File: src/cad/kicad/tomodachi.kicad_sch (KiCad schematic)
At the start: 10 parts, among them SW1 SW_SPST, U1 XIAO-ESP32-C3-DIP, U2 KY-040, U3 TC00500

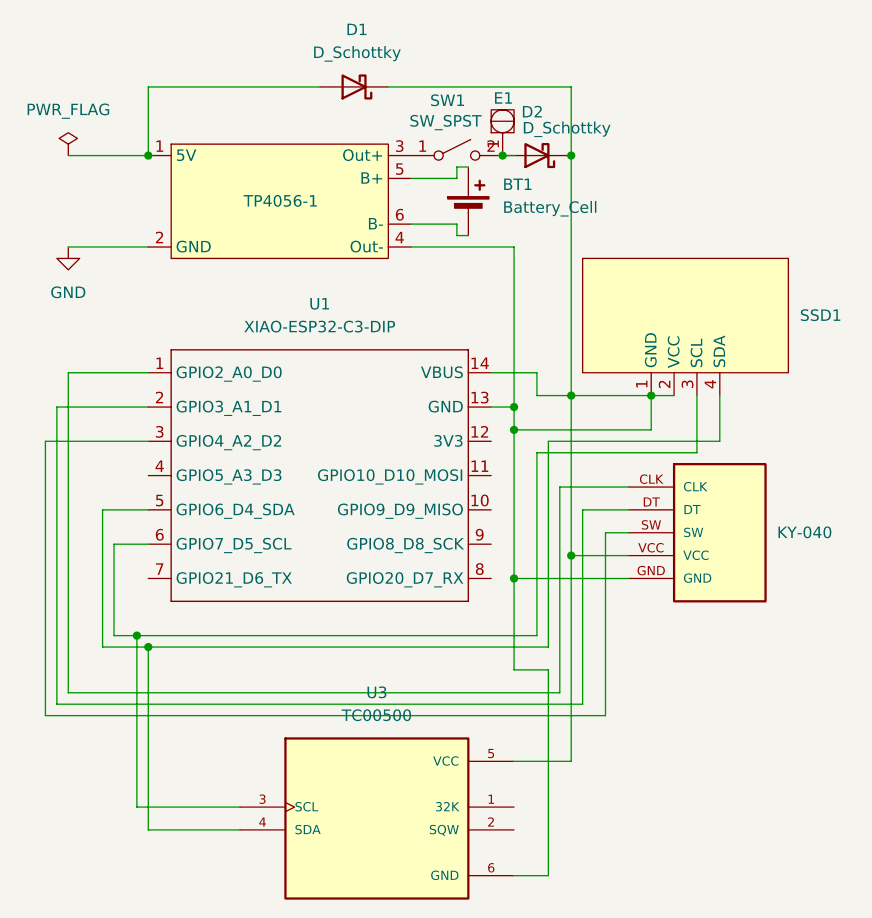
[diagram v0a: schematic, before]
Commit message: fixed PCB & added BOM and 3D files
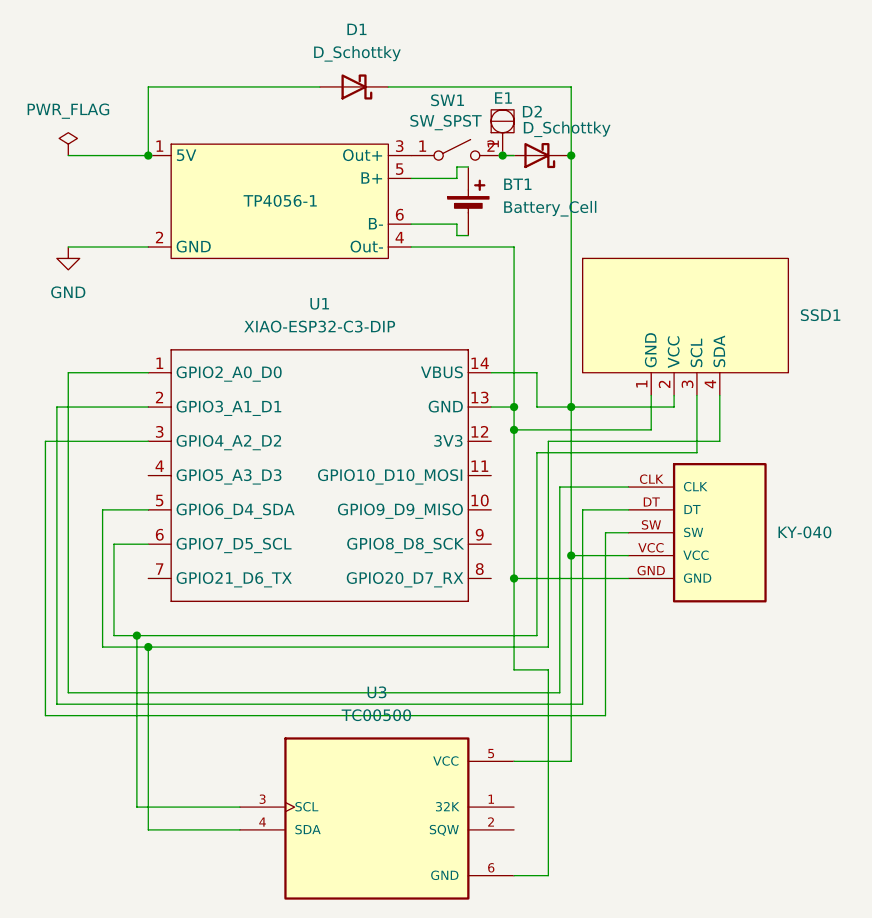
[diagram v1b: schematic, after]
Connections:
- net at D1.1 (K), D2.1 (K), SSD1.2 (VCC)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: no longer SSD1.1 (GND), TP4056-1.4 (Out-), U1.13 (GND), U2.GND, U3.6 (GND)
- new net: SSD1.1 (GND), TP4056-1.4 (Out-), U1.13 (GND), U2.GND, U3.6 (GND)
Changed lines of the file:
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@@
 	(paper "A4")
 	(junction
-		(at 120.65 81.28)
-		(diameter 0)
-		(color 0 0 0 0)
-	)
-	(junction
 		(at 113.03 54.61)
 		(diameter 0)
@@
 	)
 	(junction
+		(at 120.65 82.55)
+		(diameter 0)
+		(color 0 0 0 0)
+	)
+	(junction
 		(at 120.65 54.61)
 		(diameter 0)
@@
 	)
 	(junction
-		(at 129.54 81.28)
-		(diameter 0)
-		(color 0 0 0 0)
-	)
-	(junction
 		(at 73.66 54.61)
 		(diameter 0)
@@
 	(wire
 		(pts
+			(xy 132.08 81.28) (xy 132.08 82.55)
+		)
+		(stroke
+			(width 0)
+			(type default)
+		)
+	)
+	(wire
+		(pts
 			(xy 114.3 82.55) (xy 114.3 85.09)
 		)
@@
 	(wire
 		(pts
+			(xy 132.08 82.55) (xy 120.65 82.55)
+		)
+		(stroke
+			(width 0)
+			(type default)
+		)
+	)
+	(wire
+		(pts
 			(xy 114.3 54.61) (xy 113.03 54.61)
 		)
@@
 	(wire
 		(pts
+			(xy 120.65 82.55) (xy 120.65 99.06)
+		)
+		(stroke
+			(width 0)
+			(type default)
+		)
+	)
+	(wire
+		(pts
 			(xy 111.76 82.55) (xy 114.3 82.55)
 		)
@@
 	(wire
 		(pts
-			(xy 120.65 81.28) (xy 129.54 81.28)
-		)
-		(stroke
-			(width 0)
-			(type default)
-		)
-	)
-	(wire
-		(pts
 			(xy 116.84 107.95) (xy 72.39 107.95)
 		)
@@
 	(wire
 		(pts
+			(xy 116.84 78.74) (xy 116.84 82.55)
+		)
+		(stroke
+			(width 0)
+			(type default)
+		)
+	)
+	(wire
+		(pts
 			(xy 64.77 78.74) (xy 73.66 78.74)
 		)
@@
 	(wire
 		(pts
-			(xy 120.65 99.06) (xy 120.65 81.28)
-		)
-		(stroke
-			(width 0)
-			(type default)
-		)
-	)
-	(wire
-		(pts
-			(xy 120.65 81.28) (xy 116.84 81.28)
-		)
-		(stroke
-			(width 0)
-			(type default)
-		)
-	)
-	(wire
-		(pts
 			(xy 134.62 81.28) (xy 134.62 87.63)
 		)
@@
 	(wire
 		(pts
-			(xy 129.54 81.28) (xy 132.08 81.28)
-		)
-		(stroke
-			(width 0)
-			(type default)
-		)
-	)
-	(wire
-		(pts
-			(xy 116.84 81.28) (xy 116.84 78.74)
-		)
-		(stroke
-			(width 0)
-			(type default)
-		)
-	)
-	(wire
-		(pts
-			(xy 120.65 54.61) (xy 120.65 81.28)
+			(xy 120.65 54.61) (xy 120.65 82.55)
 		)
 		(stroke
@@
 		)
 		(stroke
+			(width 0)
+			(type default)
+		)
+	)
+	(wire
+		(pts
+			(xy 116.84 82.55) (xy 120.65 82.55)
+		)
+		(stroke
